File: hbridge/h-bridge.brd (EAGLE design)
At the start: 44.5 x 44.5 mm, 11 parts

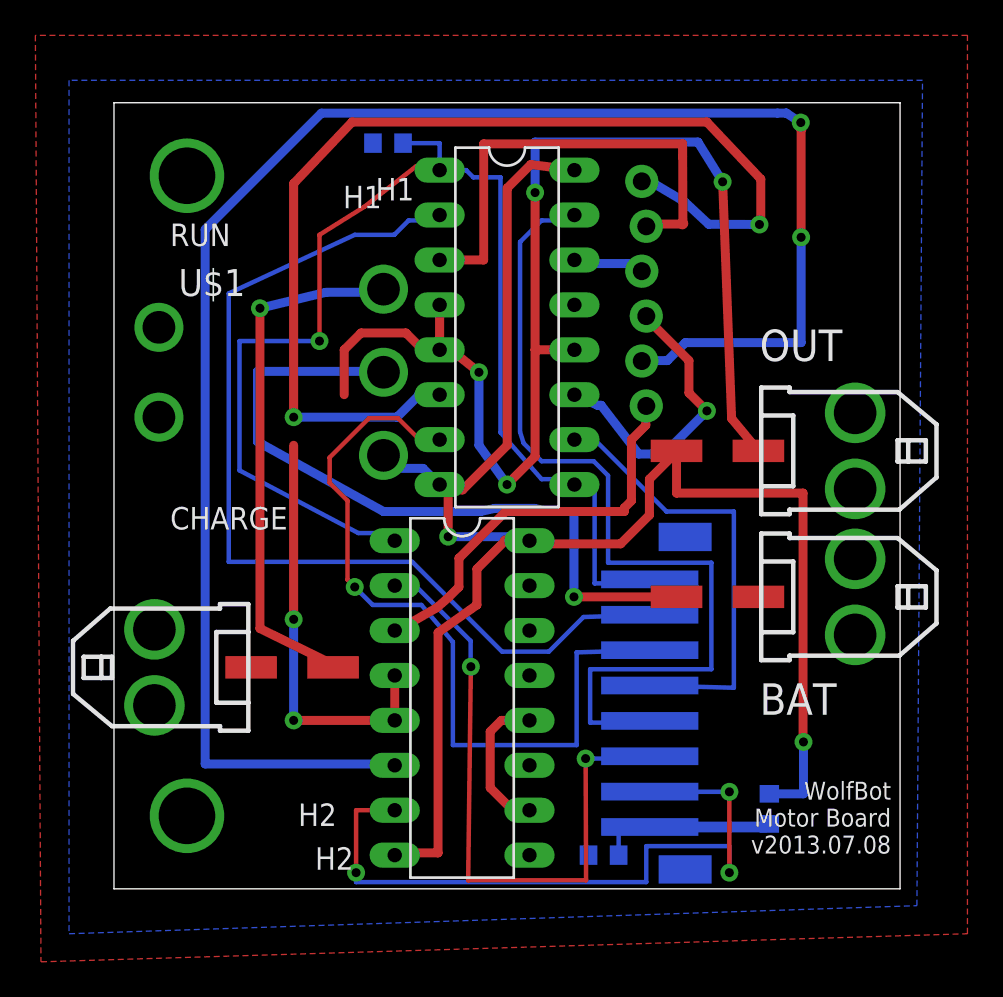
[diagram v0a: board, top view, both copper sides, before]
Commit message: Fixed PH connector footprint and resistor in way
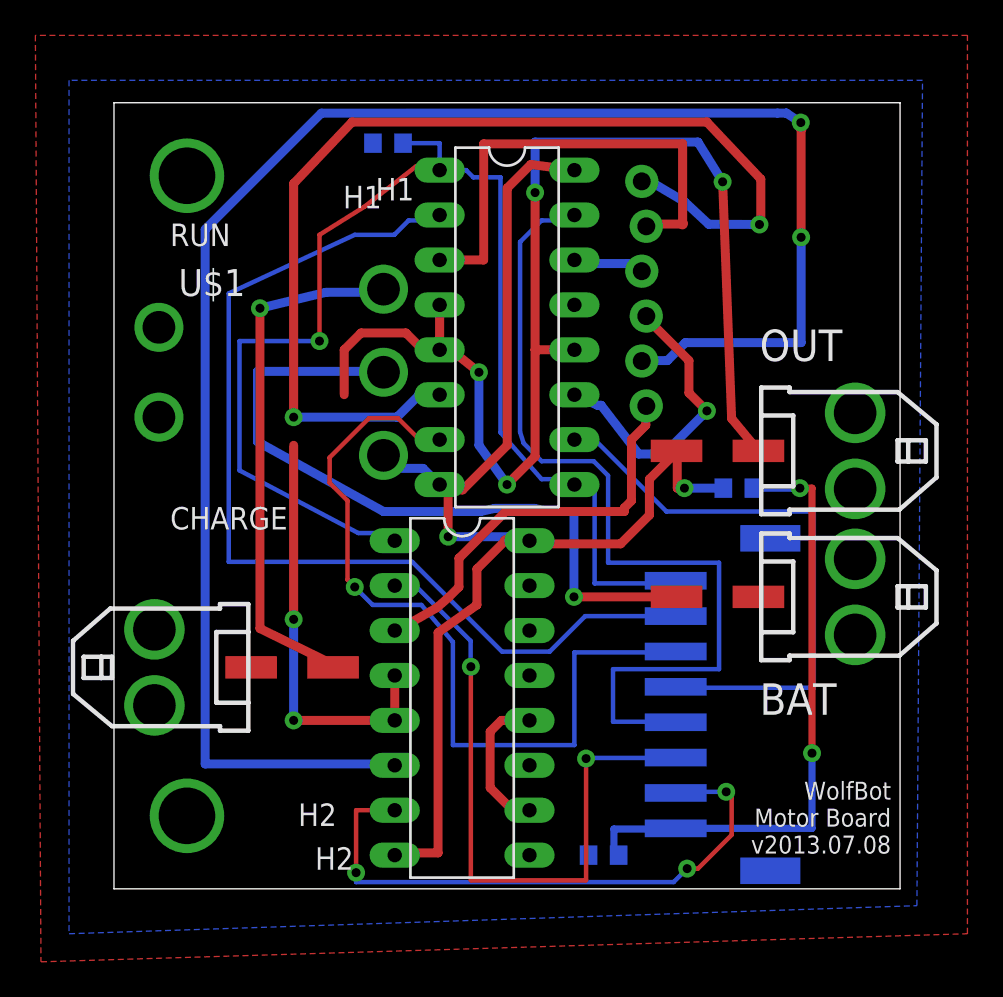
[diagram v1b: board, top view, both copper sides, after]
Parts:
- moved BATT_H 18.2 mm to (35.3, 22.7), turned to 0 degrees
- moved U$3 4.22 mm to (39.0, 20.4)
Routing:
- net N$2: track 10.0 -> 36.8 mm, vias 0 -> 2
- net V_RUN: track 99.5 -> 75.7 mm
- net M2_MOVE: track 25.4 -> 33.0 mm
- net M3_DIR: track 40.1 -> 35.5 mm
- net M3_MOVE: track 36.4 -> 38.6 mm
- net M1_DIR: track 44.7 -> 46.2 mm
- net M1_MOVE: track 55.0 -> 56.5 mm
- net ENABLE: track 73.2 -> 74.4 mm
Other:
- board text added: "B_V"
